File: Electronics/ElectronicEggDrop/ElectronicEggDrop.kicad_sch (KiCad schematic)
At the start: 13 parts

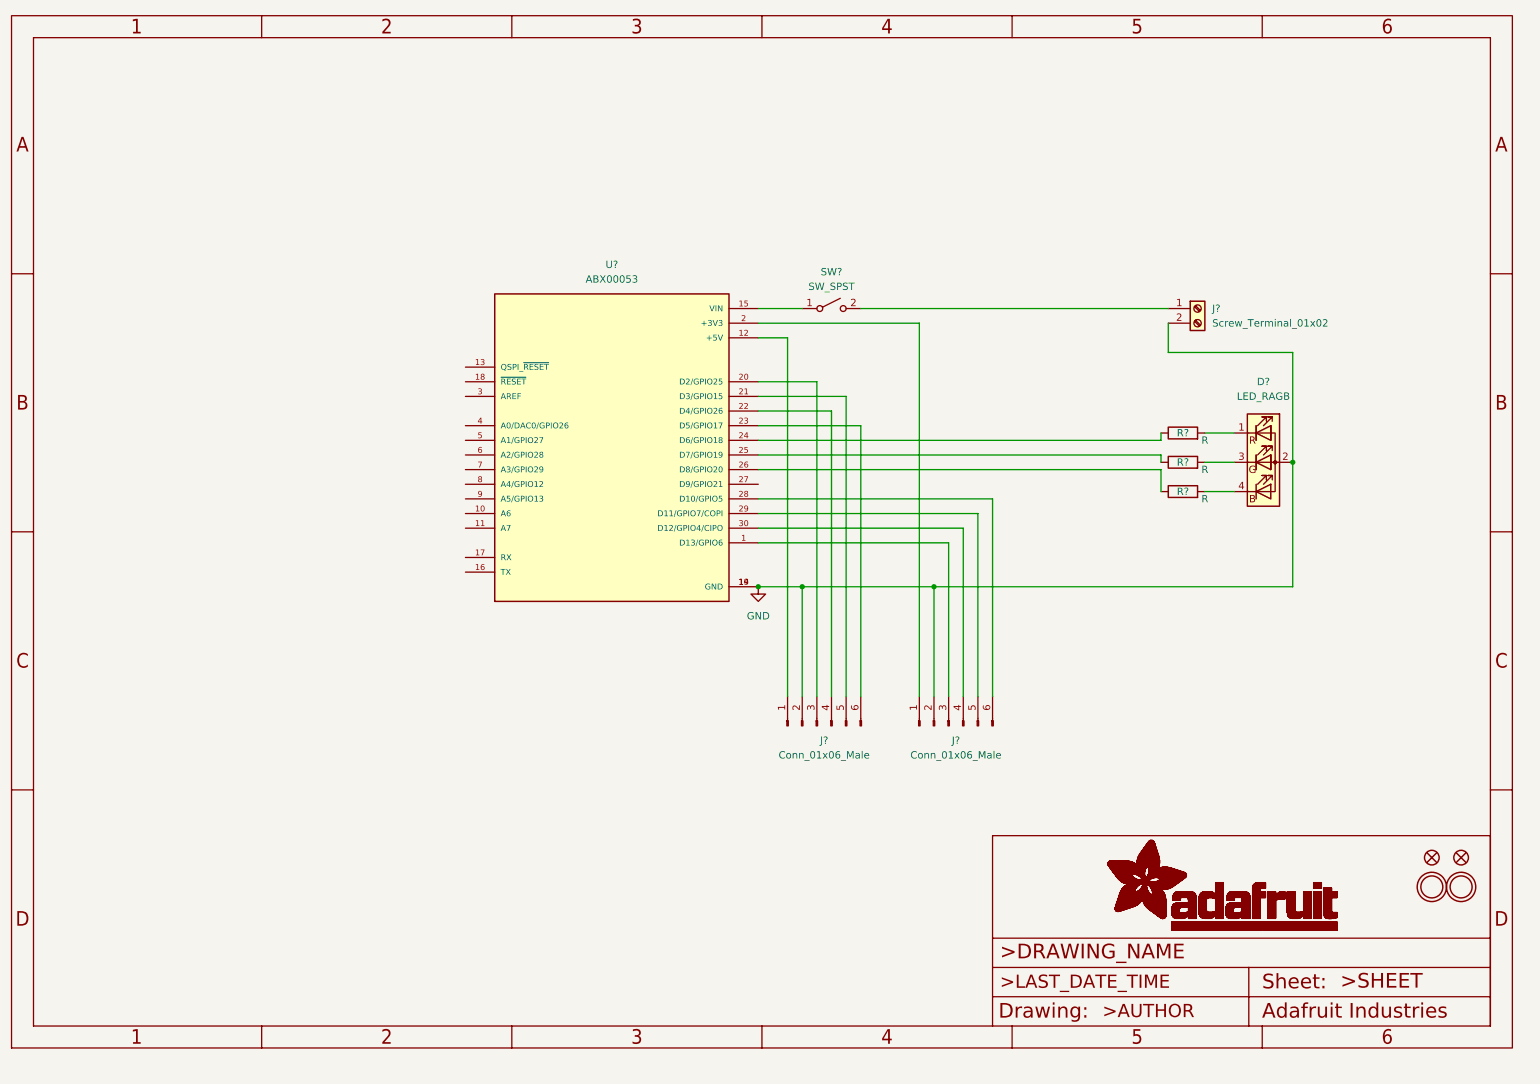
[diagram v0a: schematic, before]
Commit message: Created Egg Main board, needs different power connector. Needs secondary board
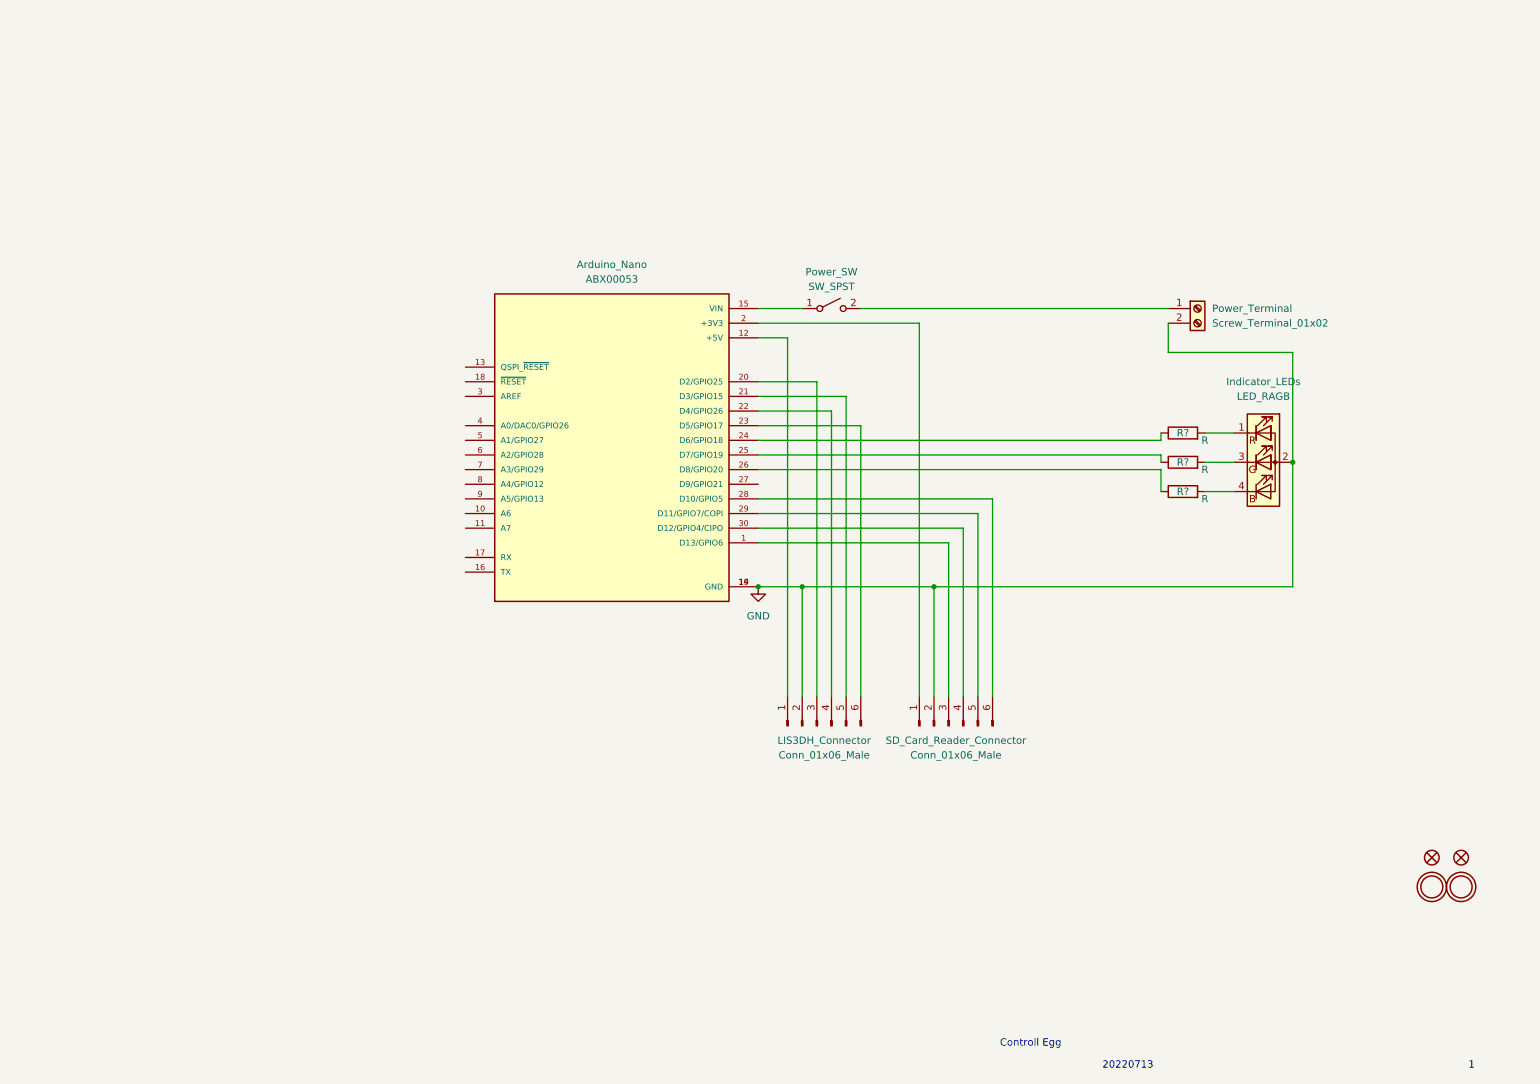
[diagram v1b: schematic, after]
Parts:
- FID1, FID2: value (none) -> FIDUCIAL{dblquote}{dblquote}; footprint (none) -> ElectronicEggDrop:FIDUCIAL_1MM
- Indicator_LEDs: renamed from D?; footprint Connector_Molex:Molex_Mega-Fit_76829-0106_2x03_P5.70mm_Vertical -> Connector_Molex:Molex_KK-254_AE-6410-04A_1x04_P2.54mm_Vertical
- LIS3DH_Connector: renamed from J?; footprint (none) -> Connector_Molex:Molex_KK-254_AE-6410-06A_1x06_P2.54mm_Vertical
- Power_SW: renamed from SW?; footprint (none) -> Connector_Molex:Molex_KK-254_AE-6410-02A_1x02_P2.54mm_Vertical
- Power_Terminal: renamed from J?; footprint (none) -> TerminalBlock_Phoenix:TerminalBlock_Phoenix_MPT-0,5-2-2.54_1x02_P2.54mm_Horizontal
- R?: footprint (none) -> Resistor_THT:R_Axial_DIN0204_L3.6mm_D1.6mm_P5.08mm_Horizontal
- U$10, U$13: value (none) -> MOUNTINGHOLE2.5; footprint (none) -> ElectronicEggDrop:MOUNTINGHOLE_2.5_PLATED
- gave numbers to parts that had none: 2
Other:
- note added: "1"
- note added: "20220713"
- note added: "Controll Egg"
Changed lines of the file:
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@@
     (stroke (width 0) (type default) (color 0 0 0 0))
   )
+  (text "1\n" (at 270.51 201.93 0)
+    (effects (font (size 1.27 1.27)) (justify left bottom))
+  )
+  (text "20220713" (at 207.01 201.93 0)
+    (effects (font (size 1.27 1.27)) (justify left bottom))
+  )
+  (text "Controll Egg\n" (at 189.23 198.12 0)
+    (effects (font (size 1.27 1.27)) (justify left bottom))
+  )
   (symbol (lib_id "ElectronicEggDrop-eagle-import:FIDUCIAL{dblquote}{dblquote}") (at 269.24 165.1 0) (unit 1)
     (in_bom yes) (on_board yes)
@@
       (effects (font (size 1.27 1.27)) hide)
     )
-    (property "Value" "" (id 1) (at 269.24 165.1 0)
-      (effects (font (size 1.27 1.27)) hide)
-    )
-    (property "Footprint" "" (id 2) (at 269.24 165.1 0)
+    (property "Value" "FIDUCIAL{dblquote}{dblquote}" (id 1) (at 269.24 165.1 0)
+      (effects (font (size 1.27 1.27)) hide)
+    )
+    (property "Footprint" "ElectronicEggDrop:FIDUCIAL_1MM" (id 2) (at 269.24 165.1 0)
       (effects (font (size 1.27 1.27)) hide)
     )
@@
       (effects (font (size 1.27 1.27)) hide)
     )
-    (property "Value" "" (id 1) (at 269.24 170.18 0)
-      (effects (font (size 1.27 1.27)) hide)
-    )
-    (property "Footprint" "" (id 2) (at 269.24 170.18 0)
+    (property "Value" "MOUNTINGHOLE2.5" (id 1) (at 269.24 170.18 0)
+      (effects (font (size 1.27 1.27)) hide)
+    )
+    (property "Footprint" "ElectronicEggDrop:MOUNTINGHOLE_2.5_PLATED" (id 2) (at 269.24 170.18 0)
       (effects (font (size 1.27 1.27)) hide)
     )
@@
     (property "Reference" "R?" (id 0) (at 220.98 91.44 90))
     (property "Value" "R" (id 1) (at 224.79 92.71 90))
-    (property "Footprint" "" (id 2) (at 220.98 93.218 90)
+    (property "Footprint" "Resistor_THT:R_Axial_DIN0204_L3.6mm_D1.6mm_P5.08mm_Horizontal" (id 2) (at 220.98 93.218 90)
       (effects (font (size 1.27 1.27)) hide)
     )
@@
     (pin "2")
   )
-  (symbol (lib_id "ElectronicEggDrop-eagle-import:FRAME_A4_ADAFRUIT") (at 17.78 198.12 0) (unit 1)
-    (in_bom yes) (on_board yes)
-    (property "Reference" "#U$1" (id 0) (at 17.78 198.12 0)
-      (effects (font (size 1.27 1.27)) hide)
-    )
-    (property "Value" "" (id 1) (at 17.78 198.12 0)
-      (effects (font (size 1.27 1.27)) hide)
-    )
-    (property "Footprint" "" (id 2) (at 17.78 198.12 0)
-      (effects (font (size 1.27 1.27)) hide)
-    )
-    (property "Datasheet" "" (id 3) (at 17.78 198.12 0)
-      (effects (font (size 1.27 1.27)) hide)
-    )
-  )
   (symbol (lib_id "ElectronicEggDrop-eagle-import:FIDUCIAL{dblquote}{dblquote}") (at 264.16 165.1 0) (unit 1)
     (in_bom yes) (on_board yes)
@@
       (effects (font (size 1.27 1.27)) hide)
     )
-    (property "Value" "" (id 1) (at 264.16 165.1 0)
-      (effects (font (size 1.27 1.27)) hide)
-    )
-    (property "Footprint" "" (id 2) (at 264.16 165.1 0)
+    (property "Value" "FIDUCIAL{dblquote}{dblquote}" (id 1) (at 264.16 165.1 0)
+      (effects (font (size 1.27 1.27)) hide)
+    )
+    (property "Footprint" "ElectronicEggDrop:FIDUCIAL_1MM" (id 2) (at 264.16 165.1 0)
       (effects (font (size 1.27 1.27)) hide)
     )
@@
   (symbol (lib_id "Switch:SW_SPST") (at 160.02 69.85 0) (unit 1)
     (in_bom yes) (on_board yes) (fields_autoplaced)
-    (property "Reference" "SW?" (id 0) (at 160.02 63.5 0))
+    (property "Reference" "Power_SW" (id 0) (at 160.02 63.5 0))
     (property "Value" "SW_SPST" (id 1) (at 160.02 66.04 0))
-    (property "Footprint" "" (id 2) (at 160.02 69.85 0)
+    (property "Footprint" "Connector_Molex:Molex_KK-254_AE-6410-02A_1x02_P2.54mm_Vertical" (id 2) (at 160.02 69.85 0)
       (effects (font (size 1.27 1.27)) hide)
     )
@@
   (symbol (lib_id "Connector:Conn_01x06_Male") (at 157.48 142.24 90) (unit 1)
     (in_bom yes) (on_board yes) (fields_autoplaced)
-    (property "Reference" "J?" (id 0) (at 158.75 144.78 90))
+    (property "Reference" "LIS3DH_Connector" (id 0) (at 158.75 144.78 90))
     (property "Value" "Conn_01x06_Male" (id 1) (at 158.75 147.32 90))
-    (property "Footprint" "" (id 2) (at 157.48 142.24 0)
+    (property "Footprint" "Connector_Molex:Molex_KK-254_AE-6410-06A_1x06_P2.54mm_Vertical" (id 2) (at 157.48 142.24 0)
       (effects (font (size 1.27 1.27)) hide)
     )
@@
   (symbol (lib_id "Connector:Screw_Terminal_01x02") (at 223.52 69.85 0) (unit 1)
     (in_bom yes) (on_board yes) (fields_autoplaced)
-    (property "Reference" "J?" (id 0) (at 226.06 69.8499 0)
+    (property "Reference" "Power_Terminal" (id 0) (at 226.06 69.8499 0)
       (effects (font (size 1.27 1.27)) (justify left))
     )
@@
       (effects (font (size 1.27 1.27)) (justify left))
     )
-    (property "Footprint" "" (id 2) (at 223.52 69.85 0)
+    (property "Footprint" "TerminalBlock_Phoenix:TerminalBlock_Phoenix_MPT-0,5-2-2.54_1x02_P2.54mm_Horizontal" (id 2) (at 223.52 69.85 0)
       (effects (font (size 1.27 1.27)) hide)
     )
@@
   (symbol (lib_id "Connector:Conn_01x06_Male") (at 180.34 142.24 90) (unit 1)
     (in_bom yes) (on_board yes) (fields_autoplaced)
-    (property "Reference" "J?" (id 0) (at 181.61 144.78 90))
+    (property "Reference" "SD_Card_Reader_Connector" (id 0) (at 181.61 144.78 90))
     (property "Value" "Conn_01x06_Male" (id 1) (at 181.61 147.32 90))
     (property "Footprint" "Connector_Molex:Molex_KK-254_AE-6410-06A_1x06_P2.54mm_Vertical" (id 2) (at 180.34 142.24 0)
@@
       (effects (font (size 1.27 1.27)) hide)
     )
-    (property "Value" "" (id 1) (at 264.16 170.18 0)
-      (effects (font (size 1.27 1.27)) hide)
-    )
-    (property "Footprint" "" (id 2) (at 264.16 170.18 0)
+    (property "Value" "MOUNTINGHOLE2.5" (id 1) (at 264.16 170.18 0)
+      (effects (font (size 1.27 1.27)) hide)
+    )
+    (property "Footprint" "ElectronicEggDrop:MOUNTINGHOLE_2.5_PLATED" (id 2) (at 264.16 170.18 0)
       (effects (font (size 1.27 1.27)) hide)
     )
@@
   (symbol (lib_id "ABX00053:ABX00053") (at 121.92 92.71 0) (unit 1)
     (in_bom yes) (on_board yes) (fields_autoplaced)
-    (property "Reference" "U?" (id 0) (at 121.92 62.23 0))
+    (property "Reference" "Arduino_Nano" (id 0) (at 121.92 62.23 0))
     (property "Value" "ABX00053" (id 1) (at 121.92 64.77 0))
     (property "Footprint" "MODULE_ABX00053" (id 2) (at 121.92 92.71 0)
@@
   (symbol (lib_id "Device:LED_RAGB") (at 234.95 96.52 0) (unit 1)
     (in_bom yes) (on_board yes) (fields_autoplaced)
-    (property "Reference" "D?" (id 0) (at 234.95 82.55 0))
+    (property "Reference" "Indicator_LEDs" (id 0) (at 234.95 82.55 0))
     (property "Value" "LED_RAGB" (id 1) (at 234.95 85.09 0))
-    (property "Footprint" "Connector_Molex:Molex_Mega-Fit_76829-0106_2x03_P5.70mm_Vertical" (id 2) (at 234.95 97.79 0)
+    (property "Footprint" "Connector_Molex:Molex_KK-254_AE-6410-04A_1x04_P2.54mm_Vertical" (id 2) (at 234.95 97.79 0)
       (effects (font (size 1.27 1.27)) hide)
     )
@@
       (reference "#PWR?") (unit 1) (value "GND") (footprint "")
     )
-    (path "/298ce1c0-ee60-4401-b4de-b9b90c899557"
-      (reference "#U$1") (unit 1) (value "FRAME_A4_ADAFRUIT") (footprint "ElectronicEggDrop:")
-    )
-    (path "/f7aa1d10-f8d1-4fe6-acb4-10abc2244f09"
-      (reference "D?") (unit 1) (value "LED_RAGB") (footprint "Connector_Molex:Molex_Mega-Fit_76829-0106_2x03_P5.70mm_Vertical")
+    (path "/e0dad96b-23b2-46bc-93d4-eedf18ddd013"
+      (reference "Arduino_Nano") (unit 1) (value "ABX00053") (footprint "MODULE_ABX00053")
     )
     (path "/0ab1aabe-6d15-4feb-8511-7c76d8512d24"
@@
       (reference "FID2") (unit 1) (value "FIDUCIAL{dblquote}{dblquote}") (footprint "ElectronicEggDrop:FIDUCIAL_1MM")
     )
+    (path "/f7aa1d10-f8d1-4fe6-acb4-10abc2244f09"
+      (reference "Indicator_LEDs") (unit 1) (value "LED_RAGB") (footprint "Connector_Molex:Molex_KK-254_AE-6410-04A_1x04_P2.54mm_Vertical")
+    )
     (path "/432a2ef5-8c4c-4a55-bf4b-ba5b90ca0b70"
-      (reference "J?") (unit 1) (value "Conn_01x06_Male") (footprint "Connector_Molex:Molex_KK-254_AE-6410-06A_1x06_P2.54mm_Vertical")
+      (reference "LIS3DH_Connector") (unit 1) (value "Conn_01x06_Male") (footprint "Connector_Molex:Molex_KK-254_AE-6410-06A_1x06_P2.54mm_Vertical")
+    )
+    (path "/3bd3481f-6f6f-4cff-8d9c-7c9dc14e3fc3"
+      (reference "Power_SW") (unit 1) (value "SW_SPST") (footprint "Connector_Molex:Molex_KK-254_AE-6410-02A_1x02_P2.54mm_Vertical")
     )
     (path "/c79642f2-5f2f-4055-93db-5cce65ec58b5"
-      (reference "J?") (unit 1) (value "Screw_Terminal_01x02") (footprint "")
-    )
-    (path "/c93ef0e7-749a-4bd6-b03c-c57ac7336301"
-      (reference "J?") (unit 1) (value "Conn_01x06_Male") (footprint "Connector_Molex:Molex_KK-254_AE-6410-06A_1x06_P2.54mm_Vertical")
+      (reference "Power_Terminal") (unit 1) (value "Screw_Terminal_01x02") (footprint "TerminalBlock_Phoenix:TerminalBlock_Phoenix_MPT-0,5-2-2.54_1x02_P2.54mm_Horizontal")
     )
     (path "/1cc56aee-2767-4a3b-9d4c-5a6627626533"
@@
       (reference "R?") (unit 1) (value "R") (footprint "Resistor_THT:R_Axial_DIN0204_L3.6mm_D1.6mm_P5.08mm_Horizontal")
     )
-    (path "/3bd3481f-6f6f-4cff-8d9c-7c9dc14e3fc3"
-      (reference "SW?") (unit 1) (value "SW_SPST") (footprint "")
+    (path "/c93ef0e7-749a-4bd6-b03c-c57ac7336301"
+      (reference "SD_Card_Reader_Connector") (unit 1) (value "Conn_01x06_Male") (footprint "Connector_Molex:Molex_KK-254_AE-6410-06A_1x06_P2.54mm_Vertical")
     )
     (path "/1d853ae8-ce78-4e5a-8c2a-2d6b4dce02f7"
@@
       (reference "U$13") (unit 1) (value "MOUNTINGHOLE2.5") (footprint "ElectronicEggDrop:MOUNTINGHOLE_2.5_PLATED")
     )
-    (path "/e0dad96b-23b2-46bc-93d4-eedf18ddd013"
-      (reference "U?") (unit 1) (value "ABX00053") (footprint "MODULE_ABX00053")
-    )
-  )
+  )

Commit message: added LIS3DH
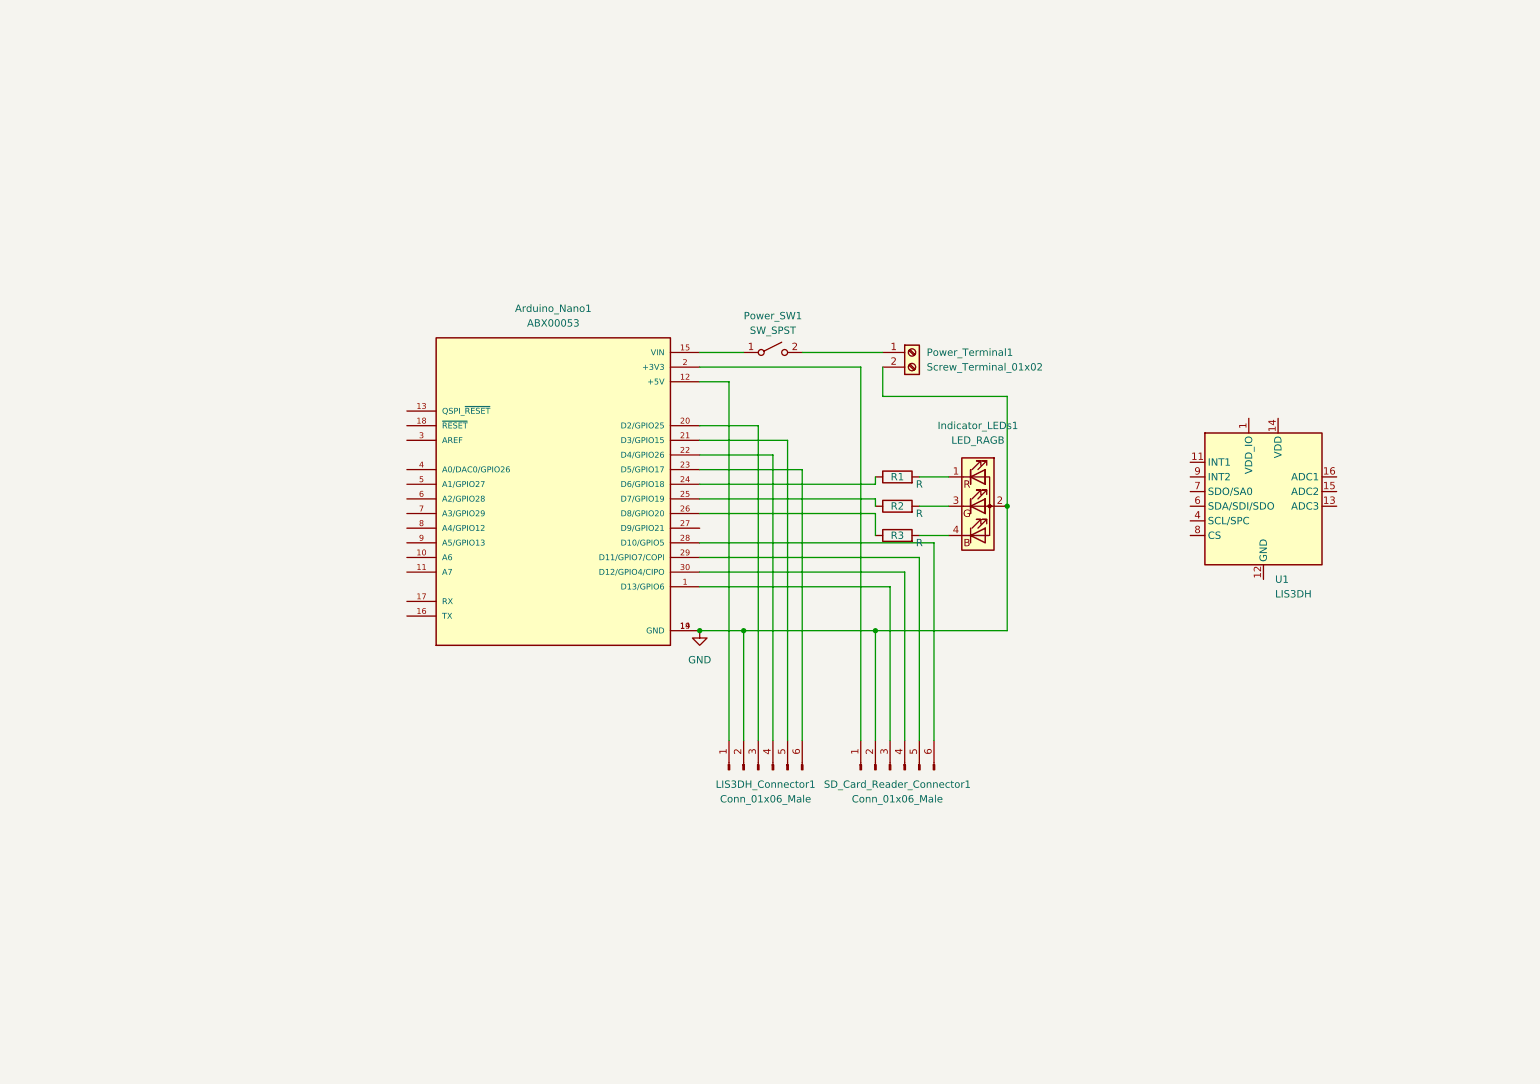
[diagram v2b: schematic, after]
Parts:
- removed FID1, FID2: FIDUCIAL{dblquote}{dblquote}, ElectronicEggDrop:FIDUCIAL_1MM, symbol ElectronicEggDrop-eagle-import:FIDUCIAL{dblquote}{dblquote}
- removed U$10, U$13: MOUNTINGHOLE2.5, ElectronicEggDrop:MOUNTINGHOLE_2.5_PLATED, symbol ElectronicEggDrop-eagle-import:MOUNTINGHOLE2.5
- added U1: LIS3DH, Package_LGA:LGA-16_3x3mm_P0.5mm_LayoutBorder3x5y, symbol Sensor_Motion:LIS3DH
- gave numbers to parts that had none: 3
- renumbered Arduino_Nano to Arduino_Nano1, Indicator_LEDs to Indicator_LEDs1, LIS3DH_Connector to LIS3DH_Connector1, Power_SW to Power_SW1, Power_Terminal to Power_Terminal1, SD_Card_Reader_Connector to SD_Card_Reader_Connector1
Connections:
- new net: U1.10 (GND), U1.12 (GND), U1.5 (GND)
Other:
- note removed: "1"
- note removed: "20220713"
- note removed: "Controll Egg"
- moved on the sheet: Arduino_Nano1, Indicator_LEDs1, LIS3DH_Connector1, Power_SW1, Power_Terminal1, R1, R2, R3, SD_Card_Reader_Connector1
